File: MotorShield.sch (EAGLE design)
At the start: 119 parts, among them IC1 OPA4340E, IC2 OPA4340E, IC3 74HCT125D, X1 MSTBV2, X2 MSTBV8, X3 MSTBV8, X4 INPUTS, X5 BUTTON_LED, X6 DOTSTARS

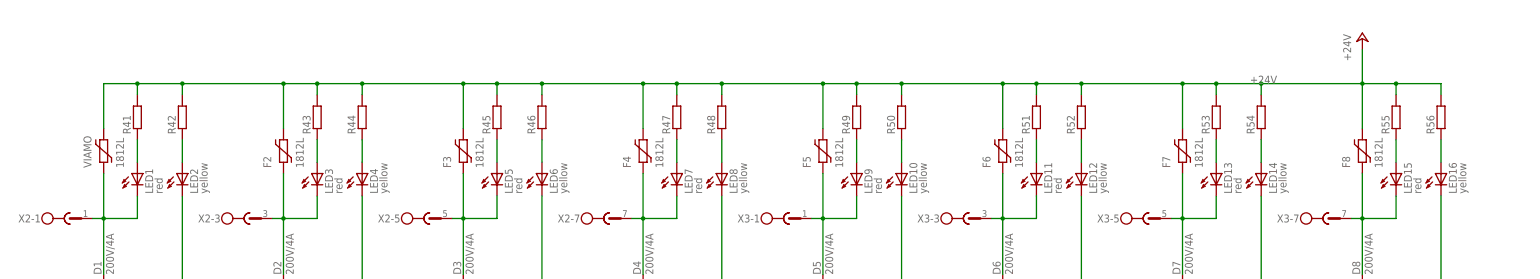
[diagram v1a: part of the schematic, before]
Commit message: assigned values to protective resistors
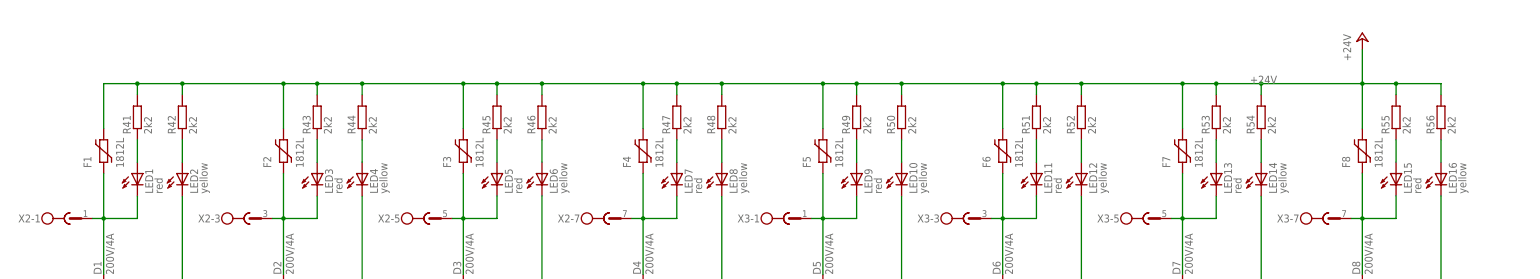
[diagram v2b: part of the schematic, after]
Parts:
- R41, R42, R43, R44, R45, R46, R47, R48, R49, R50, R51, R52, R53, R54, R55, R56: value (none) -> 2k2
- renumbered VIAMO to F1
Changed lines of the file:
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@@
 <grid distance="0.1" unitdist="inch" unit="inch" style="lines" multiple="1" display="no" altdistance="0.01" altunitdist="inch" altunit="inch"/>
 <layers>
-<layer number="1" name="Top" color="4" fill="1" visible="yes" active="no"/>
-<layer number="16" name="Bottom" color="1" fill="1" visible="yes" active="no"/>
-<layer number="17" name="Pads" color="2" fill="1" visible="yes" active="no"/>
-<layer number="18" name="Vias" color="2" fill="1" visible="yes" active="no"/>
-<layer number="19" name="Unrouted" color="6" fill="1" visible="yes" active="no"/>
-<layer number="20" name="Dimension" color="15" fill="1" visible="yes" active="no"/>
-<layer number="21" name="tPlace" color="7" fill="1" visible="yes" active="no"/>
-<layer number="22" name="bPlace" color="7" fill="1" visible="yes" active="no"/>
-<layer number="23" name="tOrigins" color="15" fill="1" visible="yes" active="no"/>
-<layer number="24" name="bOrigins" color="15" fill="1" visible="yes" active="no"/>
-<layer number="25" name="tNames" color="7" fill="1" visible="yes" active="no"/>
-<layer number="26" name="bNames" color="7" fill="1" visible="yes" active="no"/>
-<layer number="27" name="tValues" color="7" fill="1" visible="yes" active="no"/>
-<layer number="28" name="bValues" color="7" fill="1" visible="yes" active="no"/>
+<layer number="1" name="Top" color="4" fill="1" visible="no" active="no"/>
+<layer number="16" name="Bottom" color="1" fill="1" visible="no" active="no"/>
+<layer number="17" name="Pads" color="2" fill="1" visible="no" active="no"/>
+<layer number="18" name="Vias" color="2" fill="1" visible="no" active="no"/>
+<layer number="19" name="Unrouted" color="6" fill="1" visible="no" active="no"/>
+<layer number="20" name="Dimension" color="15" fill="1" visible="no" active="no"/>
+<layer number="21" name="tPlace" color="7" fill="1" visible="no" active="no"/>
+<layer number="22" name="bPlace" color="7" fill="1" visible="no" active="no"/>
+<layer number="23" name="tOrigins" color="15" fill="1" visible="no" active="no"/>
+<layer number="24" name="bOrigins" color="15" fill="1" visible="no" active="no"/>
+<layer number="25" name="tNames" color="7" fill="1" visible="no" active="no"/>
+<layer number="26" name="bNames" color="7" fill="1" visible="no" active="no"/>
+<layer number="27" name="tValues" color="7" fill="1" visible="no" active="no"/>
+<layer number="28" name="bValues" color="7" fill="1" visible="no" active="no"/>
 <layer number="29" name="tStop" color="7" fill="3" visible="no" active="no"/>
 <layer number="30" name="bStop" color="7" fill="6" visible="no" active="no"/>
@@
 <layer number="35" name="tGlue" color="7" fill="4" visible="no" active="no"/>
 <layer number="36" name="bGlue" color="7" fill="5" visible="no" active="no"/>
-<layer number="37" name="tTest" color="7" fill="1" visible="yes" active="no"/>
-<layer number="38" name="bTest" color="7" fill="1" visible="yes" active="no"/>
+<layer number="37" name="tTest" color="7" fill="1" visible="no" active="no"/>
+<layer number="38" name="bTest" color="7" fill="1" visible="no" active="no"/>
 <layer number="39" name="tKeepout" color="4" fill="11" visible="no" active="no"/>
 <layer number="40" name="bKeepout" color="1" fill="11" visible="no" active="no"/>
@@
 <layer number="44" name="Drills" color="7" fill="1" visible="no" active="no"/>
 <layer number="45" name="Holes" color="7" fill="1" visible="no" active="no"/>
-<layer number="46" name="Milling" color="3" fill="1" visible="yes" active="no"/>
-<layer number="47" name="Measures" color="7" fill="1" visible="yes" active="no"/>
-<layer number="48" name="Document" color="7" fill="1" visible="yes" active="no"/>
-<layer number="49" name="Reference" color="7" fill="1" visible="yes" active="no"/>
-<layer number="50" name="dxf" color="7" fill="1" visible="yes" active="no"/>
-<layer number="51" name="tDocu" color="7" fill="1" visible="yes" active="no"/>
-<layer number="52" name="bDocu" color="7" fill="1" visible="yes" active="no"/>
-<layer number="53" name="tGND_GNDA" color="7" fill="9" visible="yes" active="no"/>
-<layer number="54" name="bGND_GNDA" color="1" fill="9" visible="yes" active="no"/>
-<layer number="56" name="wert" color="7" fill="1" visible="yes" active="no"/>
+<layer number="46" name="Milling" color="3" fill="1" visible="no" active="no"/>
+<layer number="47" name="Measures" color="7" fill="1" visible="no" active="no"/>
+<layer number="48" name="Document" color="7" fill="1" visible="no" active="no"/>
+<layer number="49" name="Reference" color="7" fill="1" visible="no" active="no"/>
+<layer number="50" name="dxf" color="7" fill="1" visible="no" active="no"/>
+<layer number="51" name="tDocu" color="7" fill="1" visible="no" active="no"/>
+<layer number="52" name="bDocu" color="7" fill="1" visible="no" active="no"/>
+<layer number="53" name="tGND_GNDA" color="7" fill="9" visible="no" active="no"/>
+<layer number="54" name="bGND_GNDA" color="1" fill="9" visible="no" active="no"/>
+<layer number="56" name="wert" color="7" fill="1" visible="no" active="no"/>
 <layer number="90" name="Modules" color="5" fill="1" visible="yes" active="yes"/>
 <layer number="91" name="Nets" color="2" fill="1" visible="yes" active="yes"/>
@@
 <part name="X6" library="con-wago255" deviceset="233-203" device="" value="DOTSTARS"/>
 <part name="GND4" library="supply1" deviceset="GND" device=""/>
-<part name="VIAMO" library="ptc-littlefuse" deviceset="1812L" device=""/>
+<part name="F1" library="ptc-littlefuse" deviceset="1812L" device=""/>
 <part name="F2" library="ptc-littlefuse" deviceset="1812L" device=""/>
 <part name="F3" library="ptc-littlefuse" deviceset="1812L" device=""/>
@@
 <part name="LED15" library="led" deviceset="LED" device="CHIP-LED0603" value="red"/>
 <part name="LED16" library="led" deviceset="LED" device="CHIP-LED0603" value="yellow"/>
-<part name="R41" library="rcl" deviceset="R-EU_" device="R0603"/>
-<part name="R42" library="rcl" deviceset="R-EU_" device="R0603"/>
-<part name="R43" library="rcl" deviceset="R-EU_" device="R0603"/>
-<part name="R44" library="rcl" deviceset="R-EU_" device="R0603"/>
-<part name="R45" library="rcl" deviceset="R-EU_" device="R0603"/>
-<part name="R46" library="rcl" deviceset="R-EU_" device="R0603"/>
-<part name="R47" library="rcl" deviceset="R-EU_" device="R0603"/>
-<part name="R48" library="rcl" deviceset="R-EU_" device="R0603"/>
-<part name="R49" library="rcl" deviceset="R-EU_" device="R0603"/>
-<part name="R50" library="rcl" deviceset="R-EU_" device="R0603"/>
-<part name="R51" library="rcl" deviceset="R-EU_" device="R0603"/>
-<part name="R52" library="rcl" deviceset="R-EU_" device="R0603"/>
-<part name="R53" library="rcl" deviceset="R-EU_" device="R0603"/>
-<part name="R54" library="rcl" deviceset="R-EU_" device="R0603"/>
-<part name="R55" library="rcl" deviceset="R-EU_" device="R0603"/>
-<part name="R56" library="rcl" deviceset="R-EU_" device="R0603"/>
+<part name="R41" library="rcl" deviceset="R-EU_" device="R0603" value="2k2"/>
+<part name="R42" library="rcl" deviceset="R-EU_" device="R0603" value="2k2"/>
+<part name="R43" library="rcl" deviceset="R-EU_" device="R0603" value="2k2"/>
+<part name="R44" library="rcl" deviceset="R-EU_" device="R0603" value="2k2"/>
+<part name="R45" library="rcl" deviceset="R-EU_" device="R0603" value="2k2"/>
+<part name="R46" library="rcl" deviceset="R-EU_" device="R0603" value="2k2"/>
+<part name="R47" library="rcl" deviceset="R-EU_" device="R0603" value="2k2"/>
+<part name="R48" library="rcl" deviceset="R-EU_" device="R0603" value="2k2"/>
+<part name="R49" library="rcl" deviceset="R-EU_" device="R0603" value="2k2"/>
+<part name="R50" library="rcl" deviceset="R-EU_" device="R0603" value="2k2"/>
+<part name="R51" library="rcl" deviceset="R-EU_" device="R0603" value="2k2"/>
+<part name="R52" library="rcl" deviceset="R-EU_" device="R0603" value="2k2"/>
+<part name="R53" library="rcl" deviceset="R-EU_" device="R0603" value="2k2"/>
+<part name="R54" library="rcl" deviceset="R-EU_" device="R0603" value="2k2"/>
+<part name="R55" library="rcl" deviceset="R-EU_" device="R0603" value="2k2"/>
+<part name="R56" library="rcl" deviceset="R-EU_" device="R0603" value="2k2"/>
 <part name="P+3" library="supply1" deviceset="+24V" device=""/>
 <part name="GND5" library="supply1" deviceset="GND" device=""/>
@@
 <instance part="X6" gate="G$1" x="60.96" y="187.96"/>
 <instance part="GND4" gate="1" x="48.26" y="175.26"/>
-<instance part="VIAMO" gate="G$1" x="91.44" y="139.7" rot="R90"/>
+<instance part="F1" gate="G$1" x="91.44" y="139.7" rot="R90"/>
 <instance part="F2" gate="G$1" x="132.08" y="139.7" rot="R90"/>
 <instance part="F3" gate="G$1" x="172.72" y="139.7" rot="R90"/>
@@
 <junction x="91.44" y="124.46"/>
 <pinref part="X2" gate="-1" pin="1"/>
-<pinref part="VIAMO" gate="G$1" pin="1"/>
+<pinref part="F1" gate="G$1" pin="1"/>
 <pinref part="LED1" gate="G$1" pin="C"/>
 <wire x1="91.44" y1="124.46" x2="99.06" y2="124.46" width="0.1524" layer="91"/>
@@
 <pinref part="F3" gate="G$1" pin="2"/>
 <pinref part="F2" gate="G$1" pin="2"/>
-<pinref part="VIAMO" gate="G$1" pin="2"/>
+<pinref part="F1" gate="G$1" pin="2"/>
 <pinref part="P+3" gate="1" pin="+24V"/>
 <wire x1="375.92" y1="162.56" x2="375.92" y2="154.94" width="0.1524" layer="91"/>

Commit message: routed devices for M4 and M3
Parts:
- R10: device rcl:R-EU_R0805 -> rcl:R-EU_R0603
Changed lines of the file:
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@@
 <grid distance="0.1" unitdist="inch" unit="inch" style="lines" multiple="1" display="no" altdistance="0.01" altunitdist="inch" altunit="inch"/>
 <layers>
-<layer number="1" name="Top" color="4" fill="1" visible="no" active="no"/>
-<layer number="16" name="Bottom" color="1" fill="1" visible="no" active="no"/>
-<layer number="17" name="Pads" color="2" fill="1" visible="no" active="no"/>
-<layer number="18" name="Vias" color="2" fill="1" visible="no" active="no"/>
-<layer number="19" name="Unrouted" color="6" fill="1" visible="no" active="no"/>
-<layer number="20" name="Dimension" color="15" fill="1" visible="no" active="no"/>
-<layer number="21" name="tPlace" color="7" fill="1" visible="no" active="no"/>
-<layer number="22" name="bPlace" color="7" fill="1" visible="no" active="no"/>
-<layer number="23" name="tOrigins" color="15" fill="1" visible="no" active="no"/>
-<layer number="24" name="bOrigins" color="15" fill="1" visible="no" active="no"/>
-<layer number="25" name="tNames" color="7" fill="1" visible="no" active="no"/>
-<layer number="26" name="bNames" color="7" fill="1" visible="no" active="no"/>
-<layer number="27" name="tValues" color="7" fill="1" visible="no" active="no"/>
-<layer number="28" name="bValues" color="7" fill="1" visible="no" active="no"/>
+<layer number="1" name="Top" color="4" fill="1" visible="yes" active="no"/>
+<layer number="16" name="Bottom" color="1" fill="1" visible="yes" active="no"/>
+<layer number="17" name="Pads" color="2" fill="1" visible="yes" active="no"/>
+<layer number="18" name="Vias" color="2" fill="1" visible="yes" active="no"/>
+<layer number="19" name="Unrouted" color="6" fill="1" visible="yes" active="no"/>
+<layer number="20" name="Dimension" color="15" fill="1" visible="yes" active="no"/>
+<layer number="21" name="tPlace" color="7" fill="1" visible="yes" active="no"/>
+<layer number="22" name="bPlace" color="7" fill="1" visible="yes" active="no"/>
+<layer number="23" name="tOrigins" color="15" fill="1" visible="yes" active="no"/>
+<layer number="24" name="bOrigins" color="15" fill="1" visible="yes" active="no"/>
+<layer number="25" name="tNames" color="7" fill="1" visible="yes" active="no"/>
+<layer number="26" name="bNames" color="7" fill="1" visible="yes" active="no"/>
+<layer number="27" name="tValues" color="7" fill="1" visible="yes" active="no"/>
+<layer number="28" name="bValues" color="7" fill="1" visible="yes" active="no"/>
 <layer number="29" name="tStop" color="7" fill="3" visible="no" active="no"/>
 <layer number="30" name="bStop" color="7" fill="6" visible="no" active="no"/>
@@
 <layer number="35" name="tGlue" color="7" fill="4" visible="no" active="no"/>
 <layer number="36" name="bGlue" color="7" fill="5" visible="no" active="no"/>
-<layer number="37" name="tTest" color="7" fill="1" visible="no" active="no"/>
-<layer number="38" name="bTest" color="7" fill="1" visible="no" active="no"/>
+<layer number="37" name="tTest" color="7" fill="1" visible="yes" active="no"/>
+<layer number="38" name="bTest" color="7" fill="1" visible="yes" active="no"/>
 <layer number="39" name="tKeepout" color="4" fill="11" visible="no" active="no"/>
 <layer number="40" name="bKeepout" color="1" fill="11" visible="no" active="no"/>
@@
 <layer number="44" name="Drills" color="7" fill="1" visible="no" active="no"/>
 <layer number="45" name="Holes" color="7" fill="1" visible="no" active="no"/>
-<layer number="46" name="Milling" color="3" fill="1" visible="no" active="no"/>
-<layer number="47" name="Measures" color="7" fill="1" visible="no" active="no"/>
-<layer number="48" name="Document" color="7" fill="1" visible="no" active="no"/>
-<layer number="49" name="Reference" color="7" fill="1" visible="no" active="no"/>
-<layer number="50" name="dxf" color="7" fill="1" visible="no" active="no"/>
-<layer number="51" name="tDocu" color="7" fill="1" visible="no" active="no"/>
-<layer number="52" name="bDocu" color="7" fill="1" visible="no" active="no"/>
-<layer number="53" name="tGND_GNDA" color="7" fill="9" visible="no" active="no"/>
-<layer number="54" name="bGND_GNDA" color="1" fill="9" visible="no" active="no"/>
-<layer number="56" name="wert" color="7" fill="1" visible="no" active="no"/>
+<layer number="46" name="Milling" color="3" fill="1" visible="yes" active="no"/>
+<layer number="47" name="Measures" color="7" fill="1" visible="yes" active="no"/>
+<layer number="48" name="Document" color="7" fill="1" visible="yes" active="no"/>
+<layer number="49" name="Reference" color="7" fill="1" visible="yes" active="no"/>
+<layer number="50" name="dxf" color="7" fill="1" visible="yes" active="no"/>
+<layer number="51" name="tDocu" color="7" fill="1" visible="yes" active="no"/>
+<layer number="52" name="bDocu" color="7" fill="1" visible="yes" active="no"/>
+<layer number="53" name="tGND_GNDA" color="7" fill="9" visible="yes" active="no"/>
+<layer number="54" name="bGND_GNDA" color="1" fill="9" visible="yes" active="no"/>
+<layer number="56" name="wert" color="7" fill="1" visible="yes" active="no"/>
 <layer number="90" name="Modules" color="5" fill="1" visible="yes" active="yes"/>
 <layer number="91" name="Nets" color="2" fill="1" visible="yes" active="yes"/>
@@
 <part name="C4" library="eagle-ltspice" deviceset="C" device="" value="10nF"/>
 <part name="D4" library="diode" deviceset="DIODE-" device="DO214AA" value="200V/4A"/>
-<part name="R10" library="rcl" deviceset="R-EU_" device="R0805" value="100k"/>
+<part name="R10" library="rcl" deviceset="R-EU_" device="R0603" value="100k"/>
 <part name="R11" library="rcl" deviceset="R-EU_" device="R0805" value="10k"/>
 <part name="R12" library="rcl" deviceset="R-EU_" device="R0805" value="100m"/>
